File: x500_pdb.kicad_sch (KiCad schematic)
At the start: 21 parts, among them IC1 LM21305SQ_NOPB

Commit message: 4 Layers
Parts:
- added J1: Conn_01x02, Connector_AMASS:AMASS_XT60PW-M_1x02_P7.20mm_Horizontal, symbol Connector_Generic:Conn_01x02
- C_2V5, C_5V0, C_C1: footprint (none) -> Capacitor_SMD:C_0603_1608Metric_Pad1.08x0.95mm_HandSolder
- C_BOOT1: renamed from C_BOOT; footprint (none) -> Capacitor_SMD:C_0603_1608Metric_Pad1.08x0.95mm_HandSolder
- C_F1: renamed from C_F; footprint (none) -> Capacitor_SMD:C_0603_1608Metric_Pad1.08x0.95mm_HandSolder
- C_FRQ1: renamed from C_FRQ; footprint (none) -> Capacitor_SMD:C_0603_1608Metric_Pad1.08x0.95mm_HandSolder
- C_IN1: footprint (none) -> Capacitor_Tantalum_SMD:CP_EIA-7343-20_Kemet-V_HandSolder
- C_IN2: footprint (none) -> Capacitor_SMD:C_1210_3225Metric_Pad1.33x2.70mm_HandSolder
- C_IN3, C_OUT1, C_OUT2: footprint (none) -> Capacitor_SMD:C_1206_3216Metric_Pad1.33x1.80mm_HandSolder
- F1: footprint (none) -> Fuse:Fuse_1206_3216Metric
- IC1: footprint QFN50P500X500X80-29N -> LM21305:QFN50P500X500X80-29N
- L1: renamed from L; footprint (none) -> Inductor_SMD:L_7.3x7.3_H3.5
- R_C1: renamed from R_C; footprint (none) -> Resistor_SMD:R_0603_1608Metric_Pad0.98x0.95mm_HandSolder
- R_EN1: renamed from R_EN; footprint (none) -> Resistor_SMD:R_0603_1608Metric_Pad0.98x0.95mm_HandSolder
- R_F1: renamed from R_F; footprint (none) -> Capacitor_SMD:C_0201_0603Metric
- R_FB1, R_FB2: footprint (none) -> Resistor_SMD:R_0603_1608Metric_Pad0.98x0.95mm_HandSolder
- R_FRQ1: renamed from R_FRQ; footprint (none) -> Resistor_SMD:R_0603_1608Metric_Pad0.98x0.95mm_HandSolder
- R_PG1: renamed from R_PG; footprint (none) -> Resistor_SMD:R_0603_1608Metric_Pad0.98x0.95mm_HandSolder
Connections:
- net +BATT: now also J1.2 (Pin_2)
- net GND: now also IC1.29 (EP), J1.1 (Pin_1)
- net BAT+_FUSED: now reaches C_IN1.1, C_IN2.1, C_IN3.1, F1.2, IC1.1 (PVIN_1), R_F1.1
- net AGND: now reaches IC1.14 (AGND_1)
- net AGND: now also IC1.17 (AGND_2), IC1.18 (AGND_3), IC1.19 (AGND_4), IC1.20 (AGND_5), IC1.24 (AGND_6)
- net EN: now reaches IC1.15 (EN), R_EN1.2
- net FREQ: now reaches C_FRQ1.1, IC1.16 (FREQ), R_FRQ1.1
- net 2V5: now reaches C_2V5.1, IC1.21 (2V5), R_PG1.1
- net AVIN: now reaches C_F1.2, IC1.22 (AVIN_1), R_F1.2
- net PGND: now reaches IC1.7 (PGND_1)
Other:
- note added: "PGND and AGND are separated nets before being connected to the GND plane with vias"
- company: (none) -> FHDO
- title: (none) -> x500 Power Delivery Board

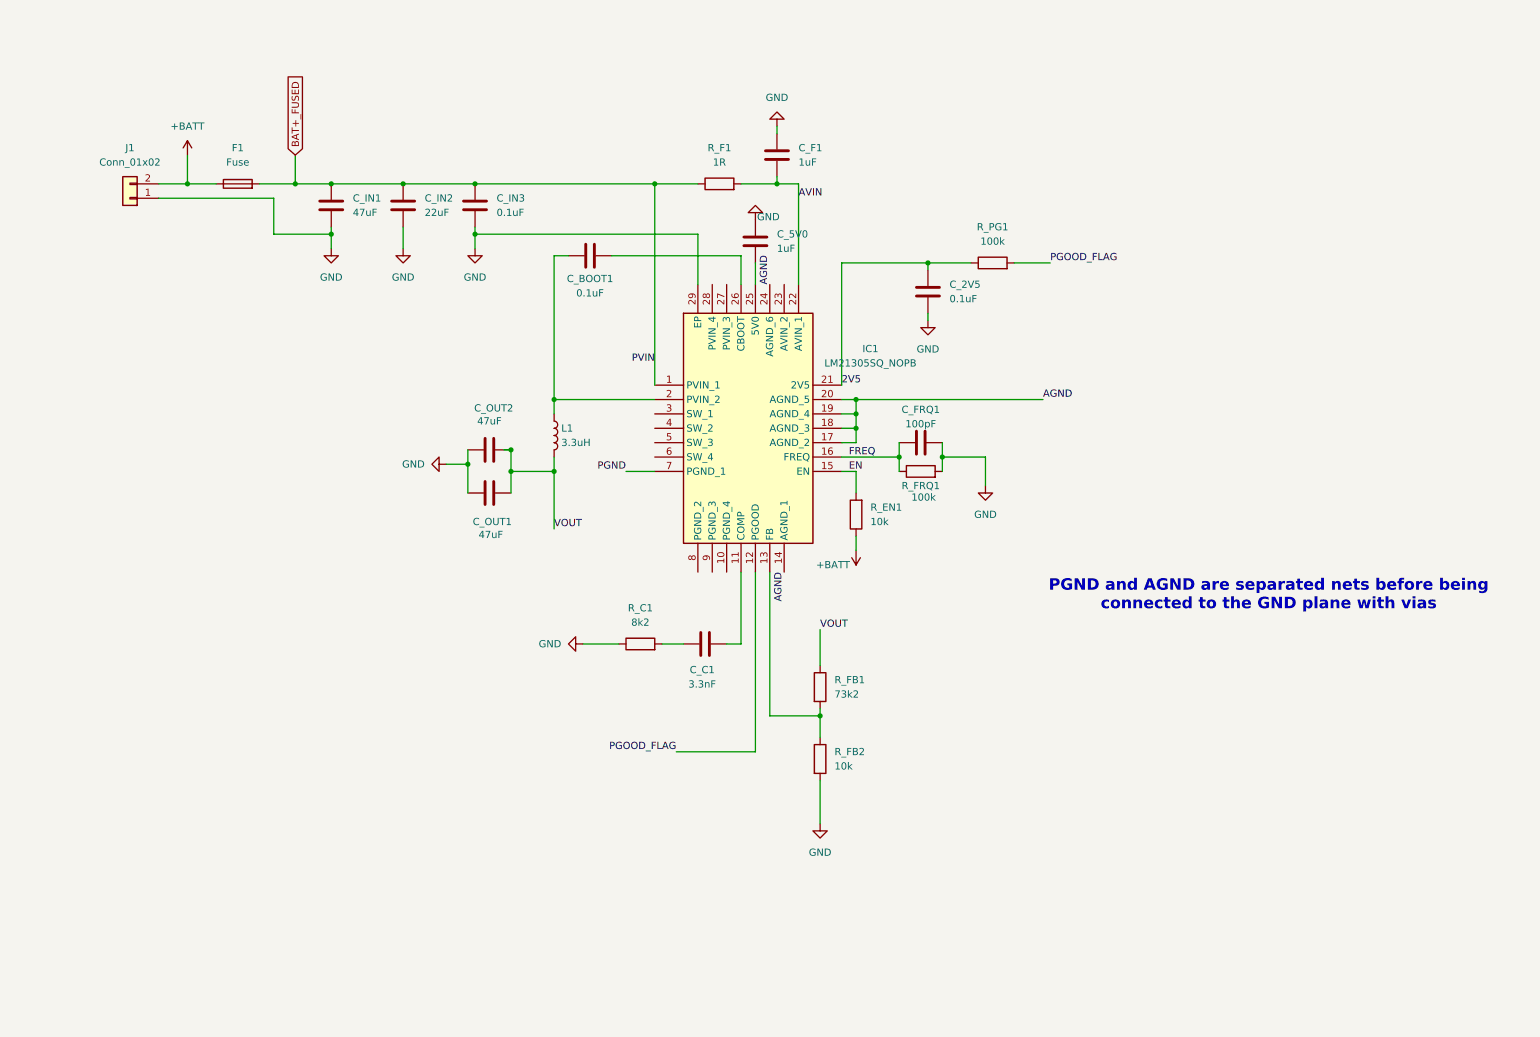
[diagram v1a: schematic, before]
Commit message: Prettying up schematics
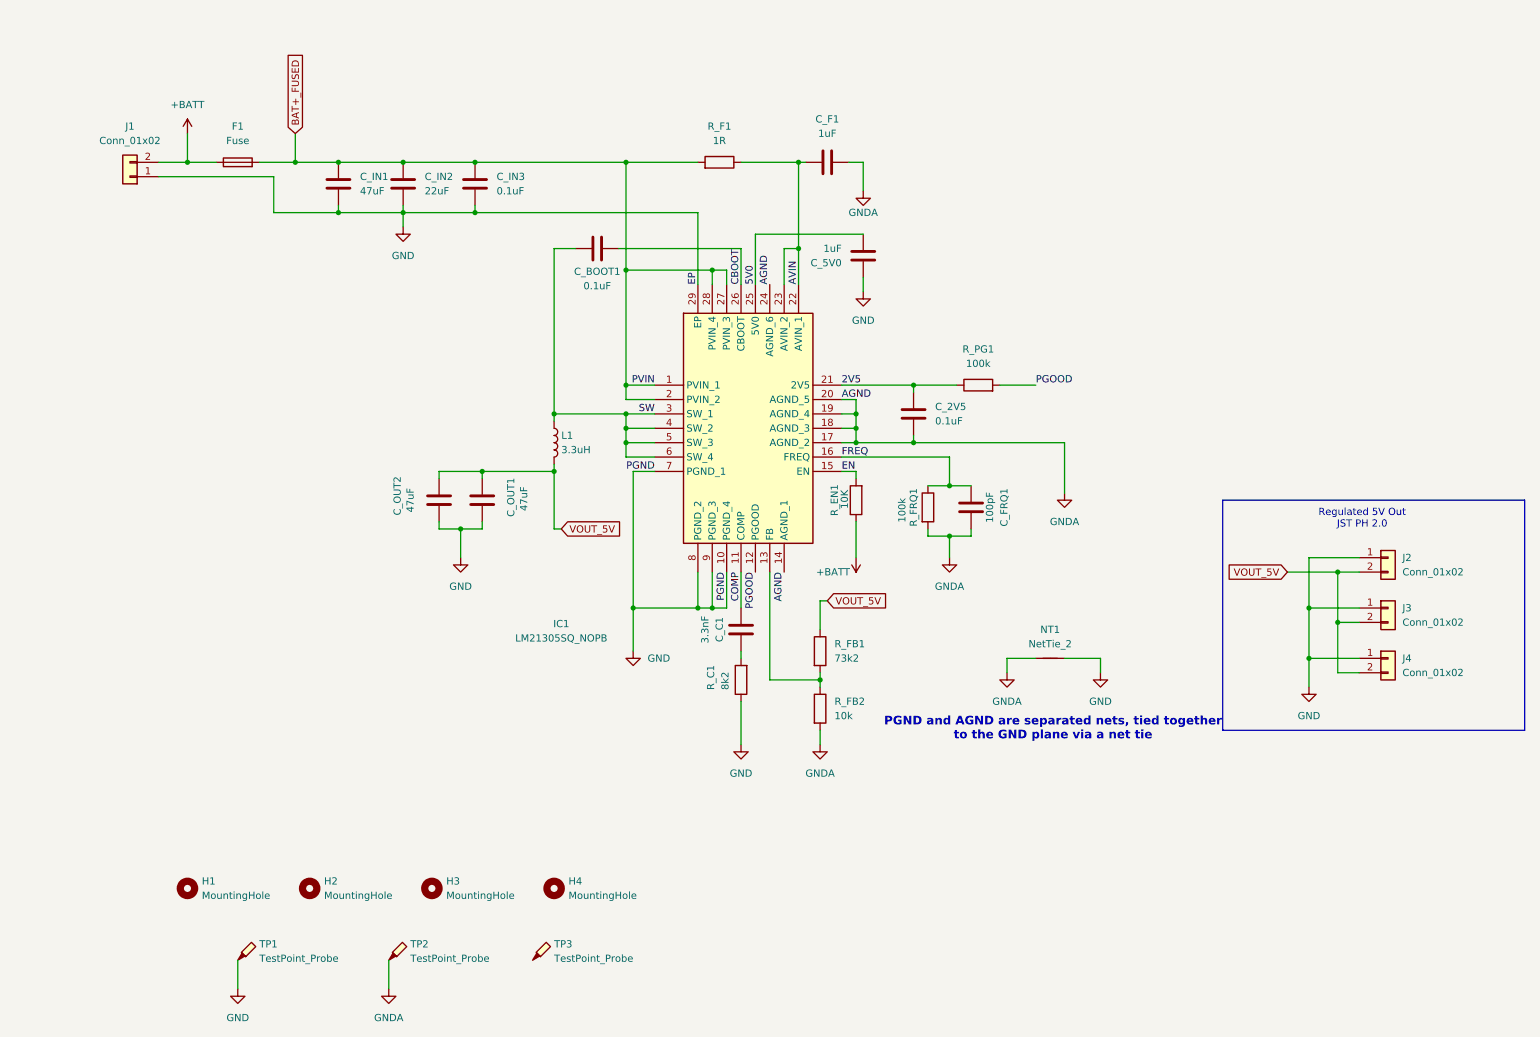
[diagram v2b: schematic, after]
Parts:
- added H1, H2, H3, H4: MountingHole, MountingHole:MountingHole_3.2mm_M3, symbol Mechanical:MountingHole
- added J2, J3, J4: Conn_01x02, Connector_JST:JST_PH_S2B-PH-K_1x02_P2.00mm_Horizontal, symbol Connector_Generic:Conn_01x02
- added NT1: NetTie_2, symbol Device:NetTie_2
- added TP1, TP2, TP3: TestPoint_Probe, TestPoint:TestPoint_Pad_1.5x1.5mm, symbol Connector:TestPoint_Probe
- J1: footprint Connector_AMASS:AMASS_XT60PW-M_1x02_P7.20mm_Horizontal -> easyeda2kicad:CONN-TH_XT60PW-M
- R_EN1: value 10k -> 10K
- R_F1: footprint Capacitor_SMD:C_0201_0603Metric -> Capacitor_SMD:C_0603_1608Metric_Pad1.08x0.95mm_HandSolder
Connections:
- net PGND is gone; now on net GND: IC1.7 (PGND_1)
- net AVIN: now also C_F1.1, IC1.23 (AVIN_2), R_F1.1; no longer C_F1.2, R_F1.2
- net BAT+_FUSED: now also IC1.2 (PVIN_2), IC1.27 (PVIN_3), IC1.28 (PVIN_4), R_F1.2; no longer R_F1.1
- net GND: now also IC1.10 (PGND_4), IC1.8 (PGND_2), IC1.9 (PGND_3), J2.1 (Pin_1), J3.1 (Pin_1), J4.1 (Pin_1), NT1.2, TP1.1; no longer C_2V5.2, C_F1.1, C_FRQ1.2, R_FB2.2, R_FRQ1.2
- net COMP: now reaches C_C1.2, IC1.11 (COMP)
- net SW: now reaches C_BOOT1.1, L1.1
- net SW: now also IC1.3 (SW_1), IC1.4 (SW_2), IC1.5 (SW_3), IC1.6 (SW_4); no longer IC1.2 (PVIN_2)
- net 5V0: now reaches C_5V0.2, IC1.25 (5V0)
- net CBOOT: now reaches C_BOOT1.2, IC1.26 (CBOOT)
- net AGND renamed GNDA
- net GNDA: now also C_2V5.2, C_F1.2, C_FRQ1.2, R_FB2.2, R_FRQ1.2, NT1.1, TP2.1
- net PGOOD_FLAG renamed PGOOD
- net VOUT renamed VOUT_5V
- net VOUT_5V: now also J2.2 (Pin_2), J3.2 (Pin_2), J4.2 (Pin_2)
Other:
- note added: "PGND and AGND are separated nets, tied together to the GND plane via a net tie"
- note added: "Regulated 5V Out JST PH 2.0"
- note removed: "PGND and AGND are separated nets before being connected to the GND plane with vias"
- moved on the sheet: C_2V5, C_5V0, C_BOOT1, C_C1, C_F1, C_FRQ1, C_IN1, C_IN2, C_IN3, C_OUT1, C_OUT2, F1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

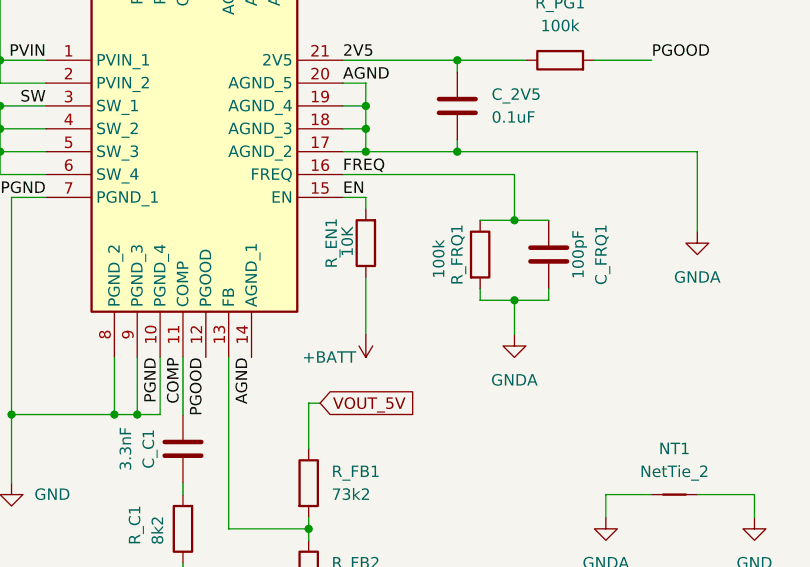
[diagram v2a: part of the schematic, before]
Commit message: Changing certain lines from +BATT to +BAT_FUSED
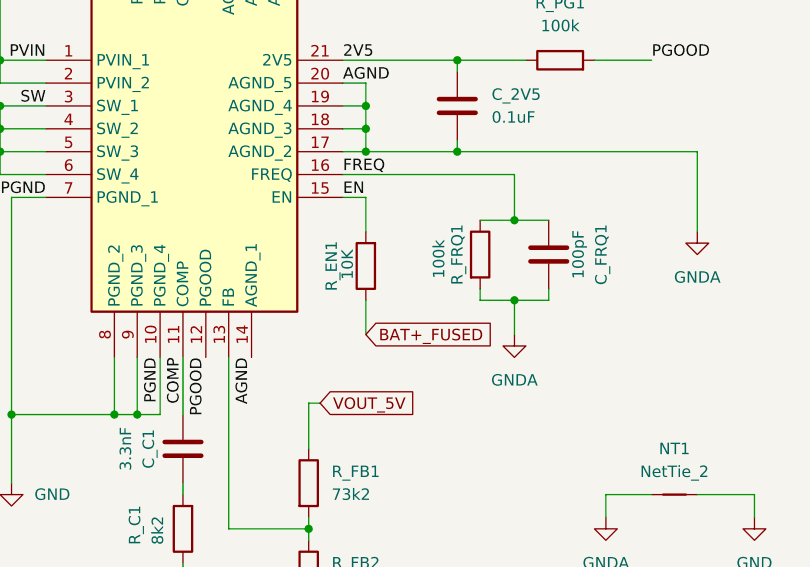
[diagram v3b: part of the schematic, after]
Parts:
- R_EN1: footprint Resistor_SMD:R_0603_1608Metric_Pad0.98x0.95mm_HandSolder -> Resistor_SMD:R_1206_3216Metric_Pad1.30x1.75mm_HandSolder
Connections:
- net +BATT: no longer R_EN1.1
- net BAT+_FUSED: now also R_EN1.1
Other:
- moved on the sheet: R_EN1
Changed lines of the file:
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@@
 	(wire
 		(pts
-			(xy 163.83 107.95) (xy 163.83 114.3)
+			(xy 163.83 110.49) (xy 163.83 114.3)
 		)
 		(stroke
@@
 	(wire
 		(pts
-			(xy 163.83 99.06) (xy 163.83 100.33)
+			(xy 163.83 99.06) (xy 163.83 102.87)
 		)
 		(stroke
@@
 		)
 	)
+	(global_label "BAT+_FUSED"
+		(shape input)
+		(at 163.83 114.3 0)
+		(fields_autoplaced yes)
+		(effects
+			(font
+				(size 1.27 1.27)
+			)
+			(justify left)
+		)
+		(property "Intersheetrefs" "${INTERSHEET_REFS}"
+			(at 178.729 114.3 0)
+			(effects
+				(font
+					(size 1.27 1.27)
+				)
+				(justify left)
+				(hide yes)
+			)
+		)
+	)
 	(global_label "VOUT_5V"
 		(shape input)
@@
 	(symbol
 		(lib_id "Device:R")
-		(at 163.83 104.14 180)
+		(at 163.83 106.68 180)
 		(unit 1)
 		(exclude_from_sim no)
@@
 		(dnp no)
 		(property "Reference" "R_EN1"
-			(at 160.02 106.934 90)
+			(at 160.02 109.474 90)
 			(effects
 				(font
@@
 		)
 		(property "Value" "10K"
-			(at 161.798 105.664 90)
+			(at 161.798 108.204 90)
 			(effects
 				(font
@@
 			)
 		)
-		(property "Footprint" "Resistor_SMD:R_0603_1608Metric_Pad0.98x0.95mm_HandSolder"
-			(at 165.608 104.14 90)
+		(property "Footprint" "Resistor_SMD:R_1206_3216Metric_Pad1.30x1.75mm_HandSolder"
+			(at 165.608 106.68 90)
 			(effects
 				(font
@@
 		)
 		(property "Datasheet" "~"
-			(at 163.83 104.14 0)
+			(at 163.83 106.68 0)
 			(effects
 				(font
@@
 		)
 		(property "Description" "Resistor"
-			(at 163.83 104.14 0)
+			(at 163.83 106.68 0)
 			(effects
 				(font
@@
 					(unit 1)
 				)
-			)
-		)
-	)
-	(symbol
-		(lib_id "power:+BATT")
-		(at 163.83 114.3 180)
-		(unit 1)
-		(exclude_from_sim no)
-		(in_bom yes)
-		(on_board yes)
-		(dnp no)
-		(property "Reference" "#PWR06"
-			(at 163.83 110.49 0)
-			(effects
-				(font
-					(size 1.27 1.27)
-				)
-				(hide yes)
-			)
-		)
-		(property "Value" "+BATT"
-			(at 159.766 116.84 0)
-			(effects
-				(font
-					(size 1.27 1.27)
-				)
-			)
-		)
-		(property "Footprint" ""
-			(at 163.83 114.3 0)
-			(effects
-				(font
-					(size 1.27 1.27)
-				)
-				(hide yes)
-			)
-		)
-		(property "Datasheet" ""
-			(at 163.83 114.3 0)
-			(effects
-				(font
-					(size 1.27 1.27)
-				)
-				(hide yes)
-			)
-		)
-		(property "Description" "Power symbol creates a global label with name \"+BATT\""
-			(at 163.83 114.3 0)
-			(effects
-				(font
-					(size 1.27 1.27)
-				)
-				(hide yes)
-			)
-		)
-		(pin "1"
-		)
-		(instances
-			(project "x500_pdb"
-				(path "/dff9cb9a-fe04-44bf-80dd-835e2154648a"
-					(reference "#PWR06")
-					(unit 1)
-				)

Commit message: Add NetTie Footprint
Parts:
- NT1: footprint (none) -> NetTie:NetTie-2_SMD_Pad2.0mm
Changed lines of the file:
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@@
 			)
 		)
-		(property "Footprint" ""
+		(property "Footprint" "NetTie:NetTie-2_SMD_Pad2.0mm"
 			(at 198.12 132.08 0)
 			(effects
